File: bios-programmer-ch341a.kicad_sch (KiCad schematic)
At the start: 51 parts, among them J1 USB_B_Micro, J2 SPI Debug, J3 I²C Debug, J4 -Banana-, J5 +Banana+, J6 ZIF16, J7 IDC, J8 IDC, J9 Terminal Block, Q1 SSM3J328R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

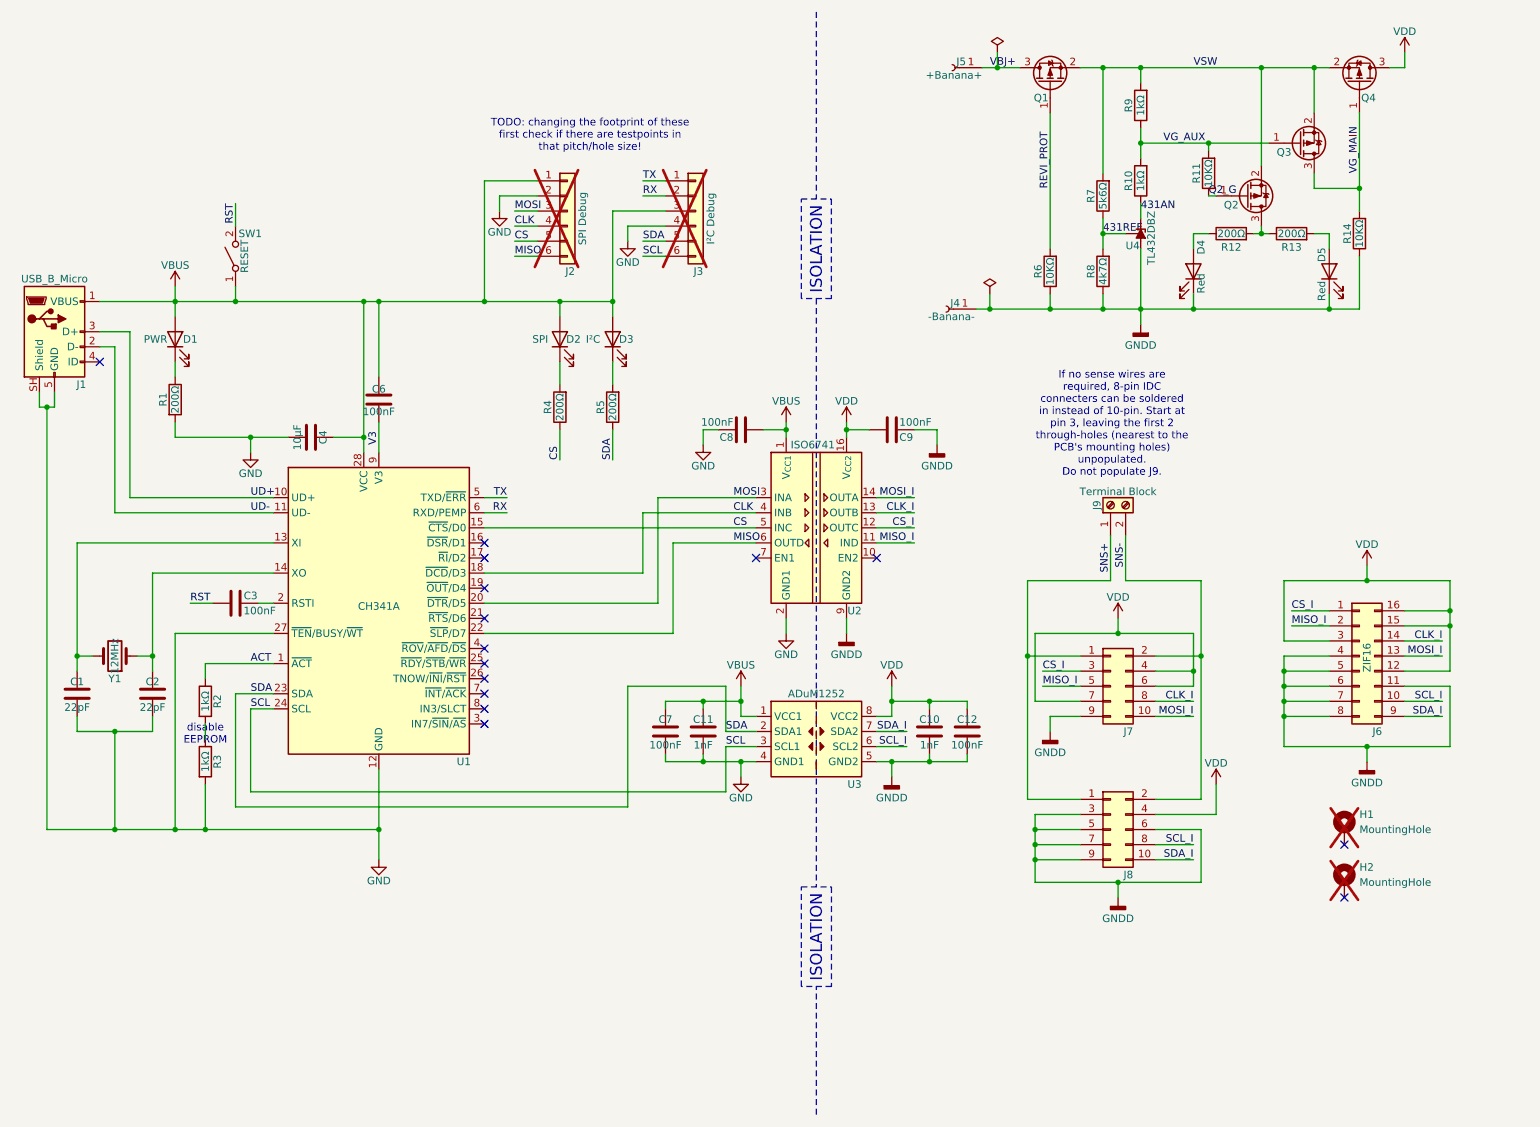
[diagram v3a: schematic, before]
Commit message: SCH/PCB: pull-up & current-limiting resistors on signal lines where needed
I don't know if this is useful let alone beneficial.
The pull-up resistors on SPI & I2C signals should theoretically improve the
current that is delivered out through the IDC connectors, right?

The current-limiting resistors may or may not be a good thing. WP and RST on
the SPI IDC connector were directly connected to VDD (the external lab power
supplies' output). In theory other ICs connected to these lines could poten-
tially be powered through them. Of course, it may reduce the current required
on these pins below the HIGH signal. If it's an issue I can always replace
these with 0-Ohm jumper resistors.

Routing isn't really nice though.
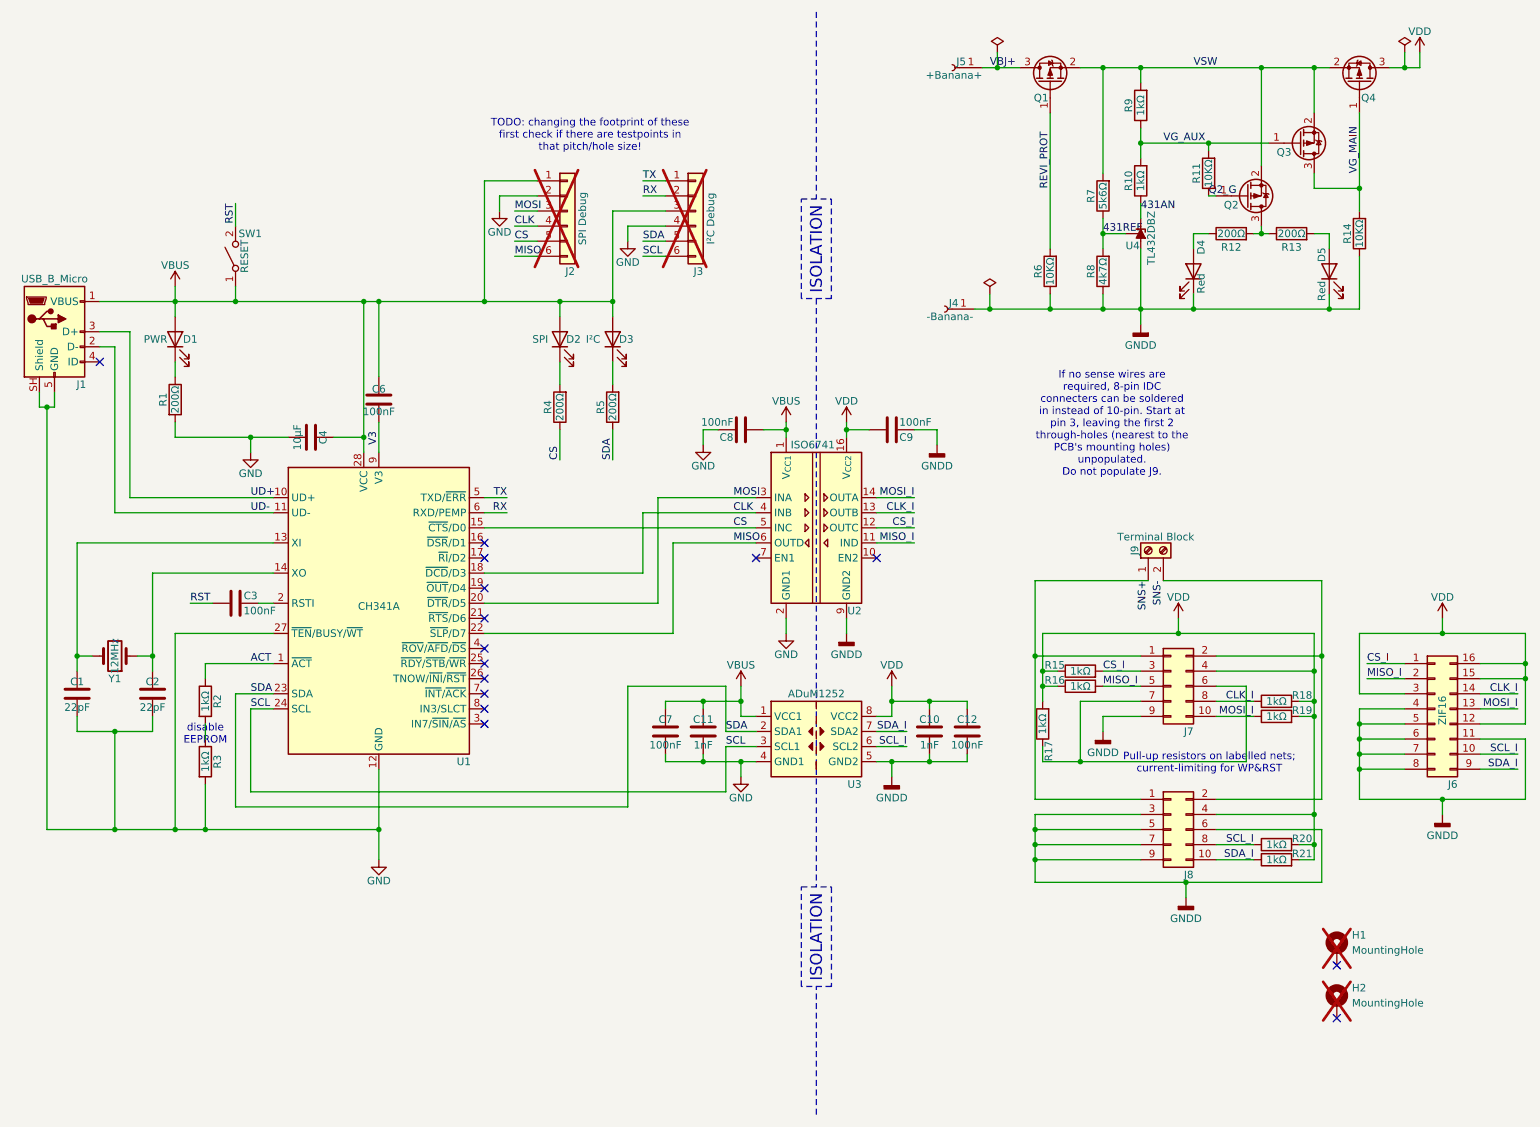
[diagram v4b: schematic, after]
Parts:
- added R15, R16, R17, R18, R19, R20, R21: 1kΩ, Resistor_SMD:R_0603_1608Metric_Pad0.98x0.95mm_HandSolder, symbol Device:R
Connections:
- net CLK_I: now also R18.1
- net CS_I: now also R15.2
- net MISO_I: now also R16.2
- net MOSI_I: now also R19.1
- net SCL_I: now also R20.1
- net SDA_I: now also R21.1
- net VDD: now also R15.1, R16.1, R17.2, R18.2, R19.2, R20.2, R21.2; no longer J7.6 (Pin_6), J7.7 (Pin_7)
- new net: J7.6 (Pin_6), J7.7 (Pin_7), R17.1
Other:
- moved on the sheet: H1, H2, J6, J7, J8, J9

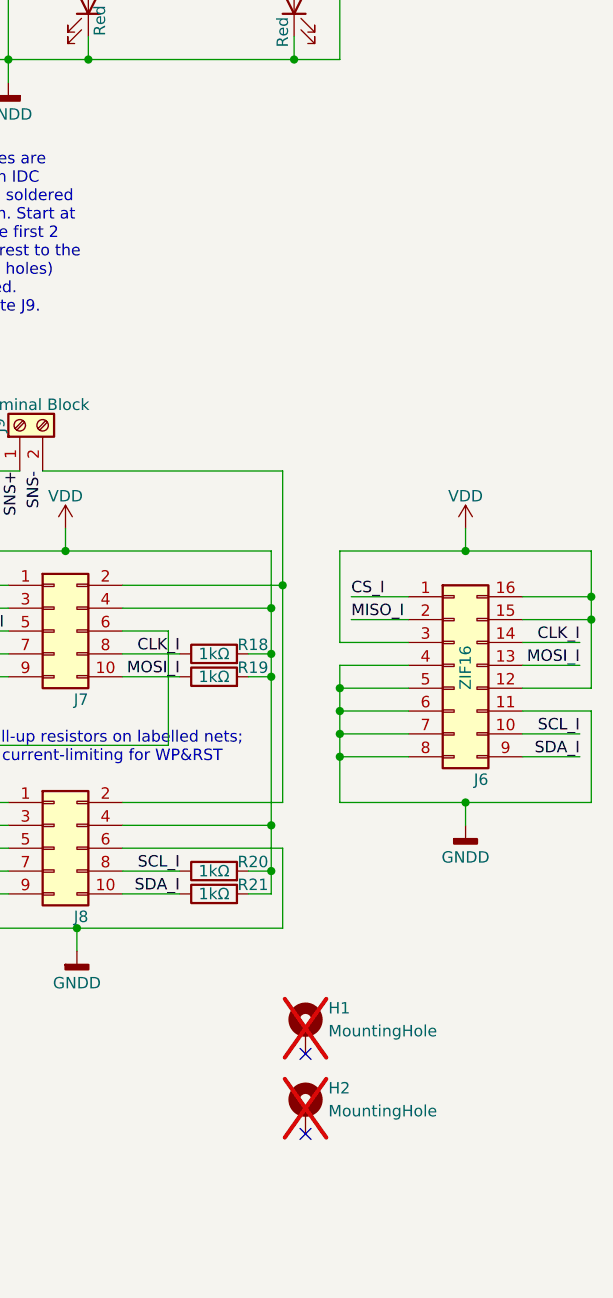
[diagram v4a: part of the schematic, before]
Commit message: PCB/SCH: updated part numbers & reset FAB layer fonts to Kicad default font
There was no reason I wanted to change the fonts for any other than the silk-
screen layers. No need to do this, it only complicates things.

Part numbers were chosen to be as cheap as possible for small-scale production
as I always do.
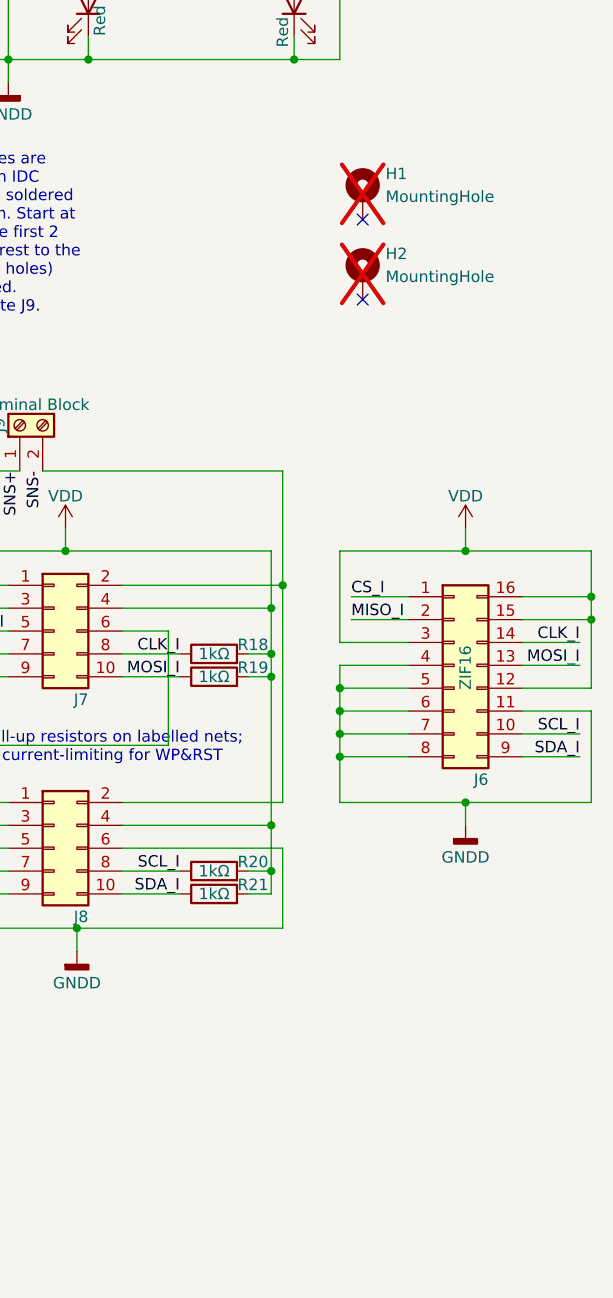
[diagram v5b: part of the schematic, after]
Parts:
- C1, C2: Part 06035A270GAT2A -> KGM15ACG1H270GT
- C10, C11: AltMfr1 Samsung -> KYOCERA AVX; AltPart1 CL10B102KB8NNNC -> 06035C102K4Z4A; Mfr Murata -> YAGEO; Part GRM033R71H102KA12D -> AC0603KRX7R0BB102
- C4: footprint Capacitor_SMD:C_1206_3216Metric_Pad1.33x1.80mm_HandSolder -> Capacitor_SMD:C_0805_2012Metric; AltMfr1 (none) -> Murata Electronics; AltPart1 (none) -> GRM21BR71A106KA73L; Mfr Taiyo Yuden -> Samsung Electro-Mechanics; Part JMK212B7106KG-T -> CL21A106KOQNNNF
- J7, J8: AltMfr1 Wurth Elektronik -> Adam Tech; AltPart1 61201021721 -> BHR-10-HUA; Mfr TE Connectivity -> Wurth Elektronik; Part 1761682-3 -> 61201021721
- J9: AltMfr1 Molex -> TE Connectivity; AltPart1 39773-0002 -> 282834-2; Mfr TE Connectivity -> GCT; Part 282834-2 -> TBC05-02-1-G-G
- R10, R15, R16, R17, R18, R19, R2, R20, R21, R3, R9: AltMfr1 (none) -> Bourns Inc; AltPart1 (none) -> CR0603-JW-102ELF
- R7: AltMfr1 (none) -> Yageo; AltPart1 (none) -> RT0603DRE075K6L
- R8: AltMfr1 (none) -> Panasonic; AltPart1 (none) -> ERA-3AEB472V; Part RR0816P-4641-D-65H -> RG1608P-472-D-T5
- U3: AltMfr1 (none) -> Analog Devices; AltPart1 (none) -> ADUM1252ASA+T
- U4: Part TL432DBZ -> TL432LIBCDBZ
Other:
- moved on the sheet: H1, H2

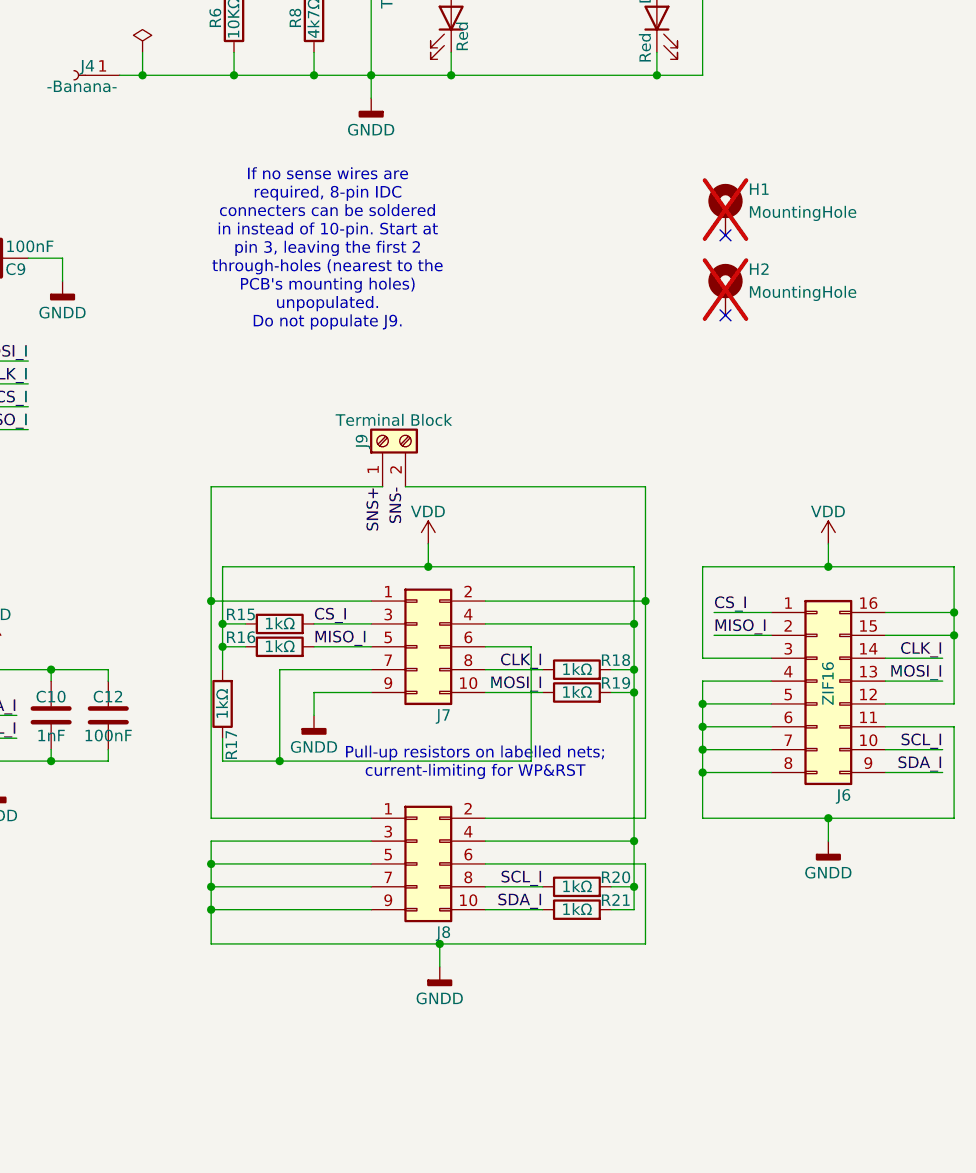
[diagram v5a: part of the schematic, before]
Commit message: 200 ohm current limiter resistor TODO calc
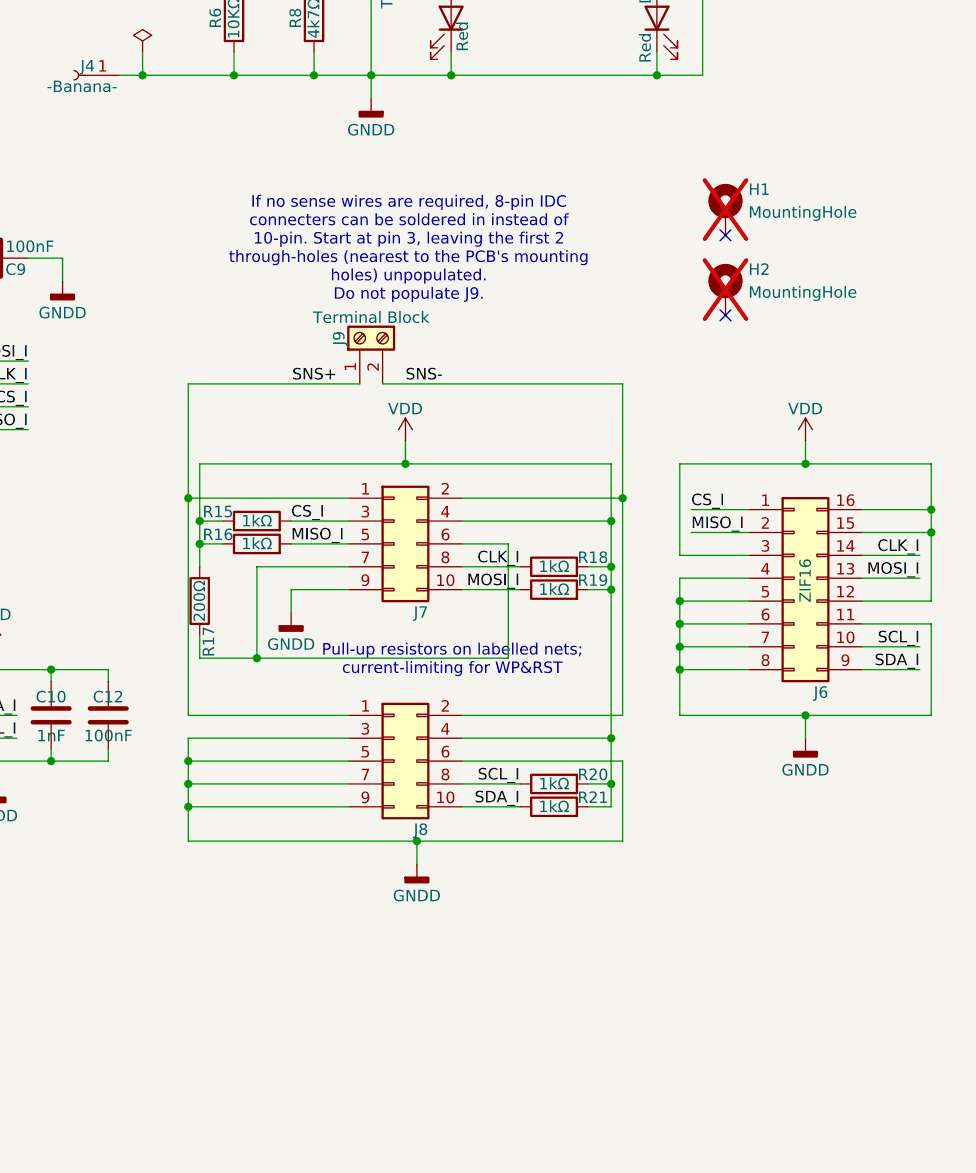
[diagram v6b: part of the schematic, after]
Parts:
- R17: value 1kΩ -> 200Ω; AltMfr1 Bourns Inc -> (none); AltPart1 CR0603-JW-102ELF -> (none); Mfr Royalohm -> Panasonic; Part CQ03WAJ0102T5E -> ERJ-3EKF2000V
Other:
- moved on the sheet: J6, J7, J8, J9, R15, R16, R18, R19, R20, R21

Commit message: SCH/PCB: 200Ohm current limiting resistor part numbers updated
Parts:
- D1: AltMfr1 Lite-On Inc -> Inolux; AltPart1 LTST-C170TBKT -> IN-S63AT5B; Mfr Inolux -> Liteon; Part IN-S85AT5B -> LTST-C194TBKT
- J9: AltMfr1 TE Connectivity -> (none); AltPart1 282834-2 -> (none)
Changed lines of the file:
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@@
 			)
 		)
-		(property "AltMfr1" "Lite-On Inc"
+		(property "AltMfr1" "Inolux"
 			(at 53.34 67.31 90)
 			(hide yes)
@@
 			)
 		)
-		(property "AltPart1" "LTST-C170TBKT"
+		(property "AltPart1" "IN-S63AT5B"
 			(at 53.34 67.31 90)
 			(hide yes)
@@
 			)
 		)
-		(property "Mfr" "Inolux"
+		(property "Mfr" "Liteon"
 			(at 53.34 67.31 90)
 			(hide yes)
@@
 			)
 		)
-		(property "Part" "IN-S85AT5B"
+		(property "Part" "LTST-C194TBKT"
 			(at 53.34 67.31 90)
 			(hide yes)
@@
 			(at 214.63 91.44 0)
 			(hide yes)
-			(show_name no)
-			(do_not_autoplace no)
-			(effects
-				(font
-					(size 1.27 1.27)
-				)
-			)
-		)
-		(property "AltMfr1" "TE Connectivity"
-			(at 214.63 91.44 0)
-			(hide yes)
-			(show_name no)
-			(do_not_autoplace no)
-			(effects
-				(font
-					(size 1.27 1.27)
-				)
-			)
-		)
-		(property "AltPart1" "282834-2"
-			(at 214.63 91.44 0)
-			(hide yes)

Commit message: permission statement ... TODO
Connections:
- net at J7.6 (Pin_6), R17.1: no longer J7.7 (Pin_7)
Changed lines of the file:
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@@
-	)
-	(junction
-		(at 203.2 127)
-		(diameter 0)
-		(color 0 0 0 0)
 	)
 	(junction
@@
 	(wire
 		(pts
-			(xy 203.2 116.84) (xy 213.36 116.84)
-		)
-		(stroke
-			(width 0)
-			(type default)
-		)
-	)
-	(wire
-		(pts
 			(xy 236.22 48.26) (xy 236.22 49.53)
 		)
@@
 	(wire
 		(pts
-			(xy 203.2 116.84) (xy 203.2 127)
-		)
-		(stroke
-			(width 0)
-			(type default)
-		)
-	)
-	(wire
-		(pts
 			(xy 132.08 43.18) (xy 135.89 43.18)
 		)
@@
 	(wire
 		(pts
-			(xy 196.85 127) (xy 203.2 127)
+			(xy 196.85 127) (xy 231.14 127)
 		)
 		(stroke
@@
 		)
 		(stroke
-			(width 0)
-			(type default)
-		)
-	)
-	(wire
-		(pts
-			(xy 203.2 127) (xy 231.14 127)
-		)
-		(stroke
